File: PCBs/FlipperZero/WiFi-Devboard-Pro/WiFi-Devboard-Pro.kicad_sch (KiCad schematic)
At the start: 26 parts

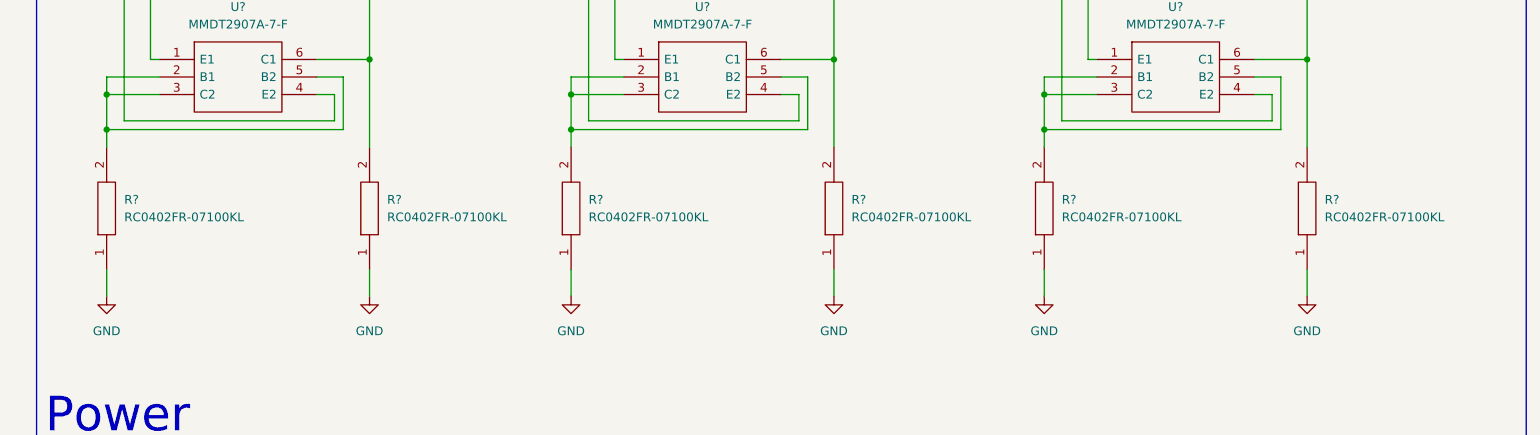
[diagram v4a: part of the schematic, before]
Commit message: Update power nets and component names
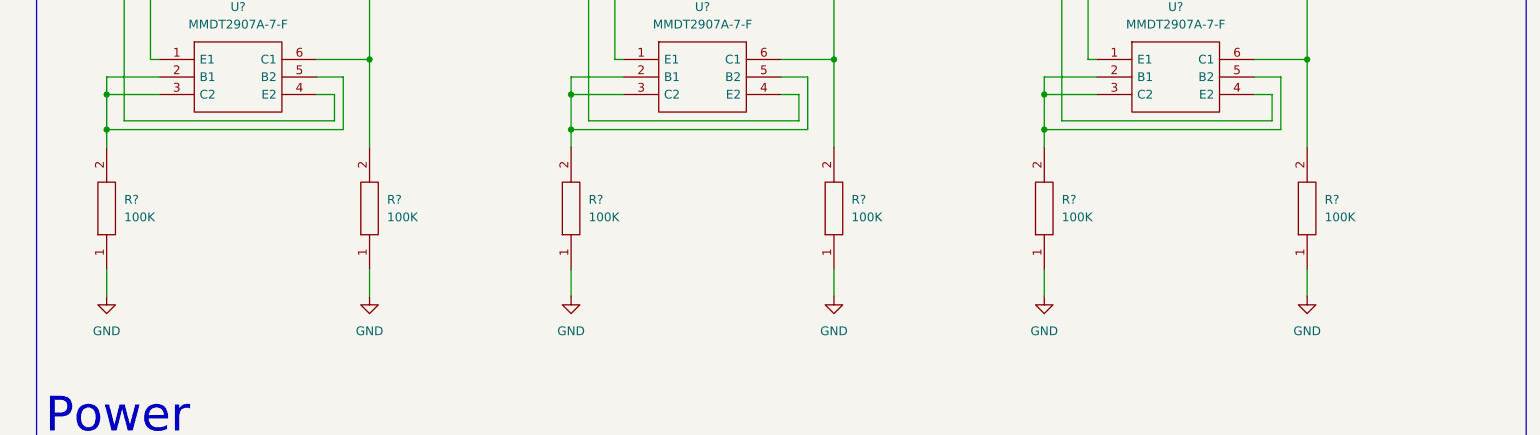
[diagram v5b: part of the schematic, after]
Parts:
- R? (x6): value RC0402FR-07100KL -> 100K
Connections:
- net +3V3: no longer C?.2, IC?.2 (OUTPUT), IC?.3 (D), IC?.3 (D), IC?.4 (VOUT), U?.4 (E2), U?.4 (E2)
- net +5V: no longer IC?.3 (D), U?.4 (E2)
- new net +LDO_3V3: C?.2, IC?.2 (OUTPUT), IC?.3 (D), IC?.4 (VOUT), U?.4 (E2)
- new net +ext_3V3: IC?.3 (D), U?.4 (E2)
- new net +ext_5V: IC?.3 (D), U?.4 (E2)
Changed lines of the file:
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@@
       (effects (font (size 1.27 1.27)) (justify right))
     )
-    (property "Value" "RC0402FR-07100KL" (id 1) (at 411.48 153.6699 90)
+    (property "Value" "100K" (id 1) (at 411.48 153.6699 90)
       (effects (font (size 1.27 1.27)) (justify right))
     )
@@
       (effects (font (size 1.27 1.27)) (justify right))
     )
-    (property "Value" "RC0402FR-07100KL" (id 1) (at 344.17 153.6699 90)
+    (property "Value" "100K" (id 1) (at 344.17 153.6699 90)
       (effects (font (size 1.27 1.27)) (justify right))
     )
@@
       (effects (font (size 1.27 1.27)) (justify right))
     )
-    (property "Value" "RC0402FR-07100KL" (id 1) (at 480.06 153.6699 90)
+    (property "Value" "100K" (id 1) (at 480.06 153.6699 90)
       (effects (font (size 1.27 1.27)) (justify right))
     )
@@
       (effects (font (size 1.27 1.27)) (justify right))
     )
-    (property "Value" "RC0402FR-07100KL" (id 1) (at 306.07 153.6699 90)
+    (property "Value" "100K" (id 1) (at 306.07 153.6699 90)
       (effects (font (size 1.27 1.27)) (justify right))
     )
@@
     (pin "1")
   )
-  (symbol (lib_name "+3V3_1") (lib_id "power:+3V3") (at 373.38 91.44 0) (unit 1)
+  (symbol (lib_name "+3V3_2") (lib_id "power:+3V3") (at 373.38 91.44 0) (unit 1)
     (in_bom yes) (on_board yes) (fields_autoplaced)
     (property "Reference" "#PWR?" (id 0) (at 373.38 95.25 0)
@@
       (effects (font (size 1.27 1.27)) (justify right))
     )
-    (property "Value" "RC0402FR-07100KL" (id 1) (at 373.38 153.6699 90)
+    (property "Value" "100K" (id 1) (at 373.38 153.6699 90)
       (effects (font (size 1.27 1.27)) (justify right))
     )
@@
       (effects (font (size 1.27 1.27)) (justify right))
     )
-    (property "Value" "RC0402FR-07100KL" (id 1) (at 441.96 153.6699 90)
+    (property "Value" "100K" (id 1) (at 441.96 153.6699 90)
       (effects (font (size 1.27 1.27)) (justify right))
     )
@@
     )
     (path "/3d7cf57e-46ad-45b0-8f37-4bcf93c58b86"
-      (reference "R?") (unit 1) (value "RC0402FR-07100KL") (footprint "RESC1005X40N")
+      (reference "R?") (unit 1) (value "100K") (footprint "RESC1005X40N")
     )
     (path "/434b8a81-ef27-4884-a038-c7022455a731"
-      (reference "R?") (unit 1) (value "RC0402FR-07100KL") (footprint "RESC1005X40N")
+      (reference "R?") (unit 1) (value "100K") (footprint "RESC1005X40N")
     )
     (path "/51956227-9277-4ca3-a264-ee96fef2edbb"
-      (reference "R?") (unit 1) (value "RC0402FR-07100KL") (footprint "RESC1005X40N")
+      (reference "R?") (unit 1) (value "100K") (footprint "RESC1005X40N")
     )
     (path "/7e45edae-6aea-4a3f-b6bd-37e282e1851a"
-      (reference "R?") (unit 1) (value "RC0402FR-07100KL") (footprint "RESC1005X40N")
+      (reference "R?") (unit 1) (value "100K") (footprint "RESC1005X40N")
     )
     (path "/e70859b0-5640-4eb1-b309-a9cceea26974"
-      (reference "R?") (unit 1) (value "RC0402FR-07100KL") (footprint "RESC1005X40N")
+      (reference "R?") (unit 1) (value "100K") (footprint "RESC1005X40N")
     )
     (path "/ed41245f-e4c9-458c-b7a4-4a54f1cc652d"
@@
     )
     (path "/f825078a-0b67-447d-a4bb-7e5f06e86419"
-      (reference "R?") (unit 1) (value "RC0402FR-07100KL") (footprint "RESC1005X40N")
+      (reference "R?") (unit 1) (value "100K") (footprint "RESC1005X40N")
     )
     (path "/032121d6-13fe-407e-b1d5-09ad6e574252"
